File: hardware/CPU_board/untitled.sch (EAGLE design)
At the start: 60 parts, among them IC1 MAX232ECWE, IC2 MAX232ECWE, IC3 AM29F040J, IC4 74HCT138D, IC5 LM2596S, J2 POWER_JACKSLT, U1 AS6C4008-55SIN, Y1 CRYSTAL-GROUNDEDSMD-5X3.2

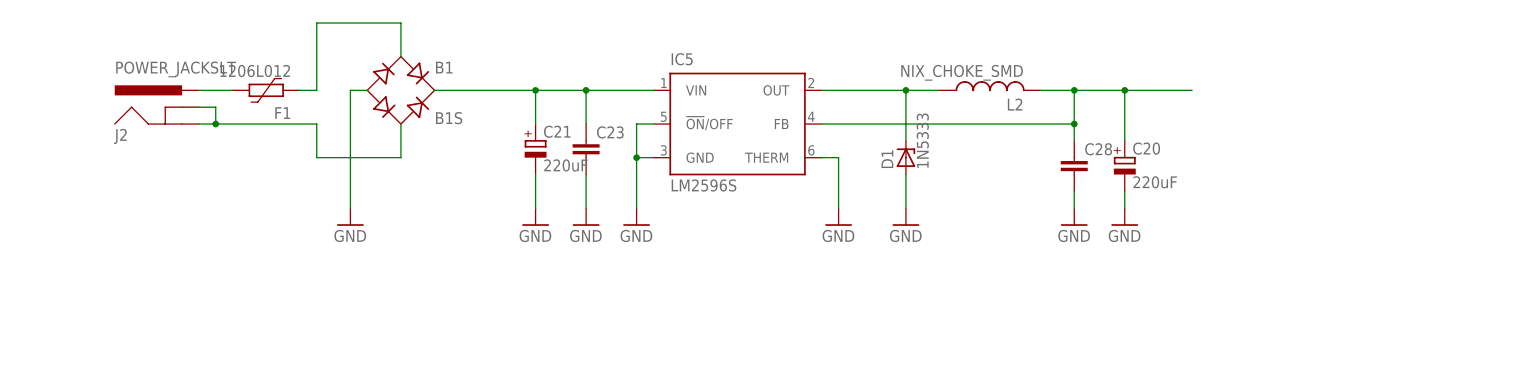
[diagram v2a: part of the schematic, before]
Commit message: Power circuit updated
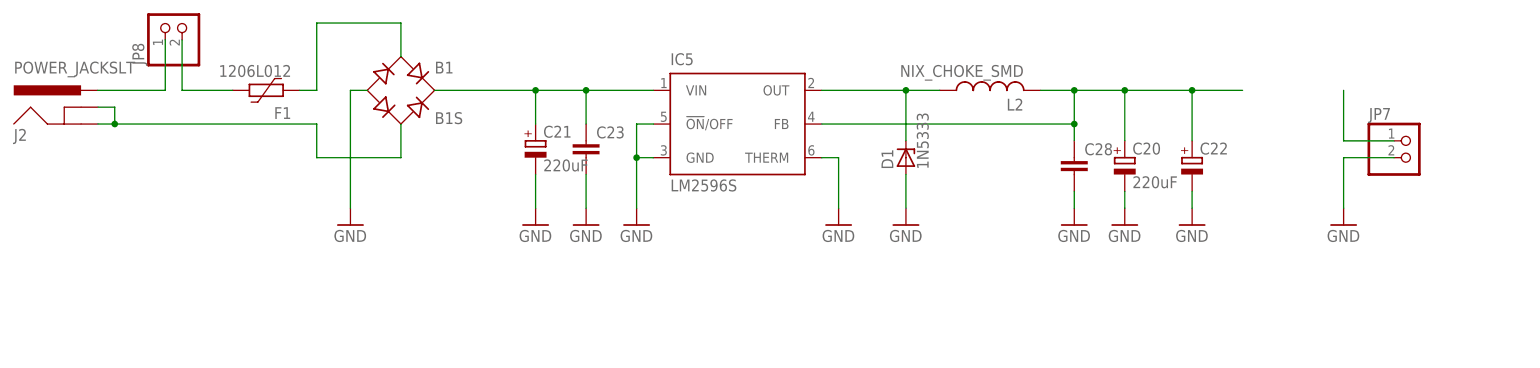
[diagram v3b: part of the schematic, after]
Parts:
- added C22: (no value), rcl:CPOL-EUSMCC
- added JP7, JP8: (no value), pinhead:PINHD-1X2
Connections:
- new net N$39: F1.1, JP8.2
- net 5V: now also C22.+, JP7.1
- net GND: now also C22.-, JP7.2
- net N$20: now also JP8.1; no longer F1.1
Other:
- moved on the sheet: J2
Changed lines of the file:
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@@
 <part name="C20" library="rcl" deviceset="CPOL-EU" device="153CLV-0810" value="220uF"/>
 <part name="L2" library="mw" deviceset="NIX_CHOKE_SMD" device=""/>
+<part name="JP7" library="pinhead" deviceset="PINHD-1X2" device=""/>
+<part name="GND18" library="supply1" deviceset="GND" device=""/>
+<part name="C22" library="rcl" deviceset="CPOL-EU" device="SMCC"/>
+<part name="GND21" library="supply1" deviceset="GND" device=""/>
+<part name="JP8" library="pinhead" deviceset="PINHD-1X2" device=""/>
 </parts>
 <sheets>
@@
 <instance part="C12" gate="G$1" x="-63.5" y="193.04"/>
 <instance part="F1" gate="G$1" x="-236.22" y="274.32" rot="R180"/>
-<instance part="J2" gate="G$1" x="-248.92" y="266.7"/>
+<instance part="J2" gate="G$1" x="-264.16" y="266.7"/>
 <instance part="GND52" gate="1" x="-195.58" y="254"/>
 <instance part="GND58" gate="1" x="-180.34" y="254"/>
@@
 <instance part="C20" gate="G$1" x="-106.68" y="264.16"/>
 <instance part="L2" gate="G$1" x="-127" y="274.32" rot="R90"/>
+<instance part="JP7" gate="G$1" x="-63.5" y="264.16"/>
+<instance part="GND18" gate="1" x="-73.66" y="254"/>
+<instance part="C22" gate="G$1" x="-96.52" y="264.16"/>
+<instance part="GND21" gate="1" x="-96.52" y="254"/>
+<instance part="JP8" gate="G$1" x="-248.92" y="284.48" rot="R90"/>
 </instances>
 <busses>
@@
 <wire x1="45.72" y1="-27.94" x2="45.72" y2="-43.18" width="0.1524" layer="91"/>
 </segment>
+<segment>
+<pinref part="JP7" gate="G$1" pin="2"/>
+<wire x1="-66.04" y1="264.16" x2="-73.66" y2="264.16" width="0.1524" layer="91"/>
+<wire x1="-73.66" y1="264.16" x2="-73.66" y2="256.54" width="0.1524" layer="91"/>
+<pinref part="GND18" gate="1" pin="GND"/>
+</segment>
+<segment>
+<pinref part="C22" gate="G$1" pin="-"/>
+<pinref part="GND21" gate="1" pin="GND"/>
+<wire x1="-96.52" y1="256.54" x2="-96.52" y2="259.08" width="0.1524" layer="91"/>
+</segment>
 </net>
 <net name="5V" class="0">
@@
 <pinref part="C28" gate="G$1" pin="1"/>
 <wire x1="-106.68" y1="274.32" x2="-96.52" y2="274.32" width="0.1524" layer="91"/>
+<wire x1="-96.52" y1="274.32" x2="-88.9" y2="274.32" width="0.1524" layer="91"/>
 <wire x1="-114.3" y1="266.7" x2="-114.3" y2="269.24" width="0.1524" layer="91"/>
 <junction x="-114.3" y="269.24"/>
@@
 <pinref part="L2" gate="G$1" pin="2"/>
 <wire x1="-119.38" y1="274.32" x2="-114.3" y2="274.32" width="0.1524" layer="91"/>
+<pinref part="C22" gate="G$1" pin="+"/>
+<wire x1="-96.52" y1="266.7" x2="-96.52" y2="274.32" width="0.1524" layer="91"/>
+<junction x="-96.52" y="274.32"/>
 </segment>
 <segment>
@@
 <label x="48.26" y="-10.16" size="1.4224" layer="95" rot="R90" xref="yes"/>
 </segment>
+<segment>
+<pinref part="JP7" gate="G$1" pin="1"/>
+<wire x1="-66.04" y1="266.7" x2="-73.66" y2="266.7" width="0.1524" layer="91"/>
+<wire x1="-73.66" y1="266.7" x2="-73.66" y2="274.32" width="0.1524" layer="91"/>
+</segment>
 </net>
 <net name="TXD1" class="0">
@@
 <segment>
 <pinref part="J2" gate="G$1" pin="PWR"/>
-<wire x1="-241.3" y1="274.32" x2="-246.38" y2="274.32" width="0.1524" layer="91"/>
-<pinref part="F1" gate="G$1" pin="1"/>
+<wire x1="-251.46" y1="274.32" x2="-261.62" y2="274.32" width="0.1524" layer="91"/>
+<pinref part="JP8" gate="G$1" pin="1"/>
+<wire x1="-251.46" y1="281.94" x2="-251.46" y2="274.32" width="0.1524" layer="91"/>
 </segment>
 </net>
@@
 <net name="N$24" class="0">
 <segment>
-<wire x1="-243.84" y1="269.24" x2="-228.6" y2="269.24" width="0.1524" layer="91"/>
+<wire x1="-259.08" y1="269.24" x2="-228.6" y2="269.24" width="0.1524" layer="91"/>
 <wire x1="-228.6" y1="269.24" x2="-228.6" y2="264.16" width="0.1524" layer="91"/>
 <pinref part="B1" gate="G$1" pin="AC2"/>
@@
 <wire x1="-215.9" y1="264.16" x2="-215.9" y2="269.24" width="0.1524" layer="91"/>
 <pinref part="J2" gate="G$1" pin="GNDBREAK"/>
-<wire x1="-246.38" y1="271.78" x2="-243.84" y2="271.78" width="0.1524" layer="91"/>
-<wire x1="-243.84" y1="271.78" x2="-243.84" y2="269.24" width="0.1524" layer="91"/>
+<wire x1="-261.62" y1="271.78" x2="-259.08" y2="271.78" width="0.1524" layer="91"/>
+<wire x1="-259.08" y1="271.78" x2="-259.08" y2="269.24" width="0.1524" layer="91"/>
 <pinref part="J2" gate="G$1" pin="GND"/>
-<wire x1="-246.38" y1="269.24" x2="-243.84" y2="269.24" width="0.1524" layer="91"/>
-<junction x="-243.84" y="269.24"/>
+<wire x1="-261.62" y1="269.24" x2="-259.08" y2="269.24" width="0.1524" layer="91"/>
+<junction x="-259.08" y="269.24"/>
 </segment>
 </net>
@@
 </segment>
 </net>
+<net name="N$39" class="0">
+<segment>
+<pinref part="F1" gate="G$1" pin="1"/>
+<wire x1="-241.3" y1="274.32" x2="-248.92" y2="274.32" width="0.1524" layer="91"/>
+<pinref part="JP8" gate="G$1" pin="2"/>
+<wire x1="-248.92" y1="281.94" x2="-248.92" y2="274.32" width="0.1524" layer="91"/>
+</segment>
+</net>

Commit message: Printer port (work in progress)
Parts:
- added JP9: (no value), pinhead-2:PINHD-2X13_2.54-SMD
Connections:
- new net /ACK: JP9.19
- new net /AFD: JP9.2
- new net /ERR: JP9.4
- new net /INIT: JP9.6
- new net /SLIN: JP9.8
- new net /STB: JP9.1
- new net BUSY: JP9.21
- new net NO_PIN: JP9.24
- new net PD0: JP9.3
- new net PD0_IN: U$1.PA0/HD0
- new net PD1: JP9.5
- new net PD1_IN: U$1.PA1/HD1
- new net PD2: JP9.7
- new net PD2_IN: U$1.PA2/HD2
- new net PD3: JP9.9
- new net PD3_IN: U$1.PA3/HD3
- new net PD4: JP9.11
- new net PD4_IN: U$1.PA4/HD4
- new net PD5: JP9.13
- new net PD5_IN: U$1.PA5/HD5
- new net PD6: JP9.15
- new net PD6_IN: U$1.PA6/HD6
- new net PD7: JP9.17
- new net PD7_IN: U$1.PA7/HD7
- new net PE: JP9.23
- new net SLCT: JP9.25
- net GND: now also JP9.10, JP9.12, JP9.14, JP9.16, JP9.18, JP9.20, JP9.22, JP9.26
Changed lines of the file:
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@@
 <part name="GND21" library="supply1" deviceset="GND" device=""/>
 <part name="JP8" library="pinhead" deviceset="PINHD-1X2" device=""/>
+<part name="JP9" library="pinhead-2" deviceset="PINHD-2X13" device="_2.54-SMD"/>
 </parts>
 <sheets>
@@
 <instance part="GND21" gate="1" x="-96.52" y="254"/>
 <instance part="JP8" gate="G$1" x="-248.92" y="284.48" rot="R90"/>
+<instance part="JP9" gate="A" x="454.66" y="274.32"/>
 </instances>
 <busses>
@@
 <wire x1="-96.52" y1="256.54" x2="-96.52" y2="259.08" width="0.1524" layer="91"/>
 </segment>
+<segment>
+<pinref part="JP9" gate="A" pin="26"/>
+<wire x1="459.74" y1="259.08" x2="469.9" y2="259.08" width="0.1524" layer="91"/>
+<label x="469.9" y="259.08" size="1.4224" layer="95" xref="yes"/>
+</segment>
+<segment>
+<pinref part="JP9" gate="A" pin="10"/>
+<wire x1="459.74" y1="279.4" x2="469.9" y2="279.4" width="0.1524" layer="91"/>
+<label x="469.9" y="279.4" size="1.4224" layer="95" xref="yes"/>
+</segment>
+<segment>
+<pinref part="JP9" gate="A" pin="12"/>
+<wire x1="459.74" y1="276.86" x2="469.9" y2="276.86" width="0.1524" layer="91"/>
+<label x="469.9" y="276.86" size="1.4224" layer="95" xref="yes"/>
+</segment>
+<segment>
+<pinref part="JP9" gate="A" pin="14"/>
+<wire x1="459.74" y1="274.32" x2="469.9" y2="274.32" width="0.1524" layer="91"/>
+<label x="469.9" y="274.32" size="1.4224" layer="95" xref="yes"/>
+</segment>
+<segment>
+<pinref part="JP9" gate="A" pin="16"/>
+<wire x1="459.74" y1="271.78" x2="469.9" y2="271.78" width="0.1524" layer="91"/>
+<label x="469.9" y="271.78" size="1.4224" layer="95" xref="yes"/>
+</segment>
+<segment>
+<pinref part="JP9" gate="A" pin="18"/>
+<wire x1="459.74" y1="269.24" x2="469.9" y2="269.24" width="0.1524" layer="91"/>
+<label x="469.9" y="269.24" size="1.4224" layer="95" xref="yes"/>
+</segment>
+<segment>
+<pinref part="JP9" gate="A" pin="20"/>
+<wire x1="459.74" y1="266.7" x2="469.9" y2="266.7" width="0.1524" layer="91"/>
+<label x="469.9" y="266.7" size="1.4224" layer="95" xref="yes"/>
+</segment>
+<segment>
+<pinref part="JP9" gate="A" pin="22"/>
+<wire x1="459.74" y1="264.16" x2="469.9" y2="264.16" width="0.1524" layer="91"/>
+<label x="469.9" y="264.16" size="1.4224" layer="95" xref="yes"/>
+</segment>
 </net>
 <net name="5V" class="0">
@@
 <pinref part="U$1" gate="G$1" pin="/MWR/PC2//RTSA"/>
 <wire x1="88.9" y1="137.16" x2="88.9" y2="144.78" width="0.1524" layer="91"/>
+<label x="88.9" y="144.78" size="1.4224" layer="95" rot="R90" xref="yes"/>
 </segment>
 </net>
@@
 </segment>
 </net>
+<net name="NO_PIN" class="0">
+<segment>
+<pinref part="JP9" gate="A" pin="24"/>
+<wire x1="459.74" y1="261.62" x2="469.9" y2="261.62" width="0.1524" layer="91"/>
+<label x="469.9" y="261.62" size="1.4224" layer="95" xref="yes"/>
+</segment>
+</net>
+<net name="/SLIN" class="0">
+<segment>
+<pinref part="JP9" gate="A" pin="8"/>
+<wire x1="459.74" y1="281.94" x2="469.9" y2="281.94" width="0.1524" layer="91"/>
+<label x="469.9" y="281.94" size="1.4224" layer="95" xref="yes"/>
+</segment>
+</net>
+<net name="/INIT" class="0">
+<segment>
+<pinref part="JP9" gate="A" pin="6"/>
+<wire x1="459.74" y1="284.48" x2="469.9" y2="284.48" width="0.1524" layer="91"/>
+<label x="469.9" y="284.48" size="1.4224" layer="95" xref="yes"/>
+</segment>
+</net>
+<net name="/ERR" class="0">
+<segment>
+<pinref part="JP9" gate="A" pin="4"/>
+<wire x1="459.74" y1="287.02" x2="469.9" y2="287.02" width="0.1524" layer="91"/>
+<label x="469.9" y="287.02" size="1.4224" layer="95" xref="yes"/>
+</segment>
+</net>
+<net name="/AFD" class="0">
+<segment>
+<pinref part="JP9" gate="A" pin="2"/>
+<wire x1="459.74" y1="289.56" x2="469.9" y2="289.56" width="0.1524" layer="91"/>
+<label x="469.9" y="289.56" size="1.4224" layer="95" xref="yes"/>
+</segment>
+</net>
+<net name="/STB" class="0">
+<segment>
+<pinref part="JP9" gate="A" pin="1"/>
+<wire x1="452.12" y1="289.56" x2="441.96" y2="289.56" width="0.1524" layer="91"/>
+<label x="441.96" y="289.56" size="1.4224" layer="95" rot="R180" xref="yes"/>
+</segment>
+</net>
+<net name="PD0" class="0">
+<segment>
+<pinref part="JP9" gate="A" pin="3"/>
+<wire x1="452.12" y1="287.02" x2="441.96" y2="287.02" width="0.1524" layer="91"/>
+<label x="441.96" y="287.02" size="1.4224" layer="95" rot="R180" xref="yes"/>
+</segment>
+</net>
+<net name="PD1" class="0">
+<segment>
+<pinref part="JP9" gate="A" pin="5"/>
+<wire x1="452.12" y1="284.48" x2="441.96" y2="284.48" width="0.1524" layer="91"/>
+<label x="441.96" y="284.48" size="1.4224" layer="95" rot="R180" xref="yes"/>
+</segment>
+</net>
+<net name="PD2" class="0">
+<segment>
+<pinref part="JP9" gate="A" pin="7"/>
+<wire x1="452.12" y1="281.94" x2="441.96" y2="281.94" width="0.1524" layer="91"/>
+<label x="441.96" y="281.94" size="1.4224" layer="95" rot="R180" xref="yes"/>
+</segment>
+</net>
+<net name="PD3" class="0">
+<segment>
+<pinref part="JP9" gate="A" pin="9"/>
+<wire x1="452.12" y1="279.4" x2="441.96" y2="279.4" width="0.1524" layer="91"/>
+<label x="441.96" y="279.4" size="1.4224" layer="95" rot="R180" xref="yes"/>
+</segment>
+</net>
+<net name="PD4" class="0">
+<segment>
+<pinref part="JP9" gate="A" pin="11"/>
+<wire x1="452.12" y1="276.86" x2="441.96" y2="276.86" width="0.1524" layer="91"/>
+<label x="441.96" y="276.86" size="1.4224" layer="95" rot="R180" xref="yes"/>
+</segment>
+</net>
+<net name="PD5" class="0">
+<segment>
+<pinref part="JP9" gate="A" pin="13"/>
+<wire x1="452.12" y1="274.32" x2="441.96" y2="274.32" width="0.1524" layer="91"/>
+<label x="441.96" y="274.32" size="1.4224" layer="95" rot="R180" xref="yes"/>
+</segment>
+</net>
+<net name="PD6" class="0">
+<segment>
+<pinref part="JP9" gate="A" pin="15"/>
+<wire x1="452.12" y1="271.78" x2="441.96" y2="271.78" width="0.1524" layer="91"/>
+<label x="441.96" y="271.78" size="1.4224" layer="95" rot="R180" xref="yes"/>
+</segment>
+</net>
+<net name="PD7" class="0">
+<segment>
+<pinref part="JP9" gate="A" pin="17"/>
+<wire x1="452.12" y1="269.24" x2="441.96" y2="269.24" width="0.1524" layer="91"/>
+<label x="441.96" y="269.24" size="1.4224" layer="95" rot="R180" xref="yes"/>
+</segment>
+</net>
+<net name="/ACK" class="0">
+<segment>
+<pinref part="JP9" gate="A" pin="19"/>
+<wire x1="452.12" y1="266.7" x2="441.96" y2="266.7" width="0.1524" layer="91"/>
+<label x="441.96" y="266.7" size="1.4224" layer="95" rot="R180" xref="yes"/>
+</segment>
+</net>
+<net name="BUSY" class="0">
+<segment>
+<pinref part="JP9" gate="A" pin="21"/>
+<wire x1="452.12" y1="264.16" x2="441.96" y2="264.16" width="0.1524" layer="91"/>
+<label x="441.96" y="264.16" size="1.4224" layer="95" rot="R180" xref="yes"/>
+</segment>
+</net>
+<net name="PE" class="0">
+<segment>
+<pinref part="JP9" gate="A" pin="23"/>
+<wire x1="452.12" y1="261.62" x2="441.96" y2="261.62" width="0.1524" layer="91"/>
+<label x="441.96" y="261.62" size="1.4224" layer="95" rot="R180" xref="yes"/>
+</segment>
+</net>
+<net name="SLCT" class="0">
+<segment>
+<pinref part="JP9" gate="A" pin="25"/>
+<wire x1="452.12" y1="259.08" x2="441.96" y2="259.08" width="0.1524" layer="91"/>
+<label x="441.96" y="259.08" size="1.4224" layer="95" rot="R180" xref="yes"/>
+</segment>
+</net>
+<net name="PD0_IN" class="0">
+<segment>
+<pinref part="U$1" gate="G$1" pin="PA0/HD0"/>
+<wire x1="114.3" y1="137.16" x2="114.3" y2="144.78" width="0.1524" layer="91"/>
+<label x="114.3" y="144.78" size="1.4224" layer="95" rot="R90" xref="yes"/>
+</segment>
+</net>
+<net name="PD1_IN" class="0">
+<segment>
+<pinref part="U$1" gate="G$1" pin="PA1/HD1"/>
+<wire x1="111.76" y1="137.16" x2="111.76" y2="144.78" width="0.1524" layer="91"/>
+<label x="111.76" y="144.78" size="1.4224" layer="95" rot="R90" xref="yes"/>
+</segment>
+</net>
+<net name="PD2_IN" class="0">
+<segment>
+<pinref part="U$1" gate="G$1" pin="PA2/HD2"/>
+<wire x1="109.22" y1="137.16" x2="109.22" y2="144.78" width="0.1524" layer="91"/>
+<label x="109.22" y="144.78" size="1.4224" layer="95" rot="R90" xref="yes"/>
+</segment>
+</net>
+<net name="PD3_IN" class="0">
+<segment>
+<pinref part="U$1" gate="G$1" pin="PA3/HD3"/>
+<wire x1="106.68" y1="137.16" x2="106.68" y2="144.78" width="0.1524" layer="91"/>
+<label x="106.68" y="144.78" size="1.4224" layer="95" rot="R90" xref="yes"/>
+</segment>
+</net>
+<net name="PD4_IN" class="0">
+<segment>
+<pinref part="U$1" gate="G$1" pin="PA4/HD4"/>
+<wire x1="104.14" y1="137.16" x2="104.14" y2="144.78" width="0.1524" layer="91"/>
+<label x="104.14" y="144.78" size="1.4224" layer="95" rot="R90" xref="yes"/>
+</segment>
+</net>
+<net name="PD5_IN" class="0">
+<segment>
+<pinref part="U$1" gate="G$1" pin="PA5/HD5"/>
+<wire x1="101.6" y1="137.16" x2="101.6" y2="144.78" width="0.1524" layer="91"/>
+<label x="101.6" y="144.78" size="1.4224" layer="95" rot="R90" xref="yes"/>
+</segment>
+</net>
+<net name="PD6_IN" class="0">
+<segment>
+<pinref part="U$1" gate="G$1" pin="PA6/HD6"/>
+<wire x1="99.06" y1="137.16" x2="99.06" y2="144.78" width="0.1524" layer="91"/>
+<label x="99.06" y="144.78" size="1.4224" layer="95" rot="R90" xref="yes"/>
+</segment>
+</net>
+<net name="PD7_IN" class="0">
+<segment>
+<pinref part="U$1" gate="G$1" pin="PA7/HD7"/>
+<wire x1="96.52" y1="137.16" x2="96.52" y2="144.78" width="0.1524" layer="91"/>
+<label x="96.52" y="144.78" size="1.4224" layer="95" rot="R90" xref="yes"/>
+</segment>
+</net>
